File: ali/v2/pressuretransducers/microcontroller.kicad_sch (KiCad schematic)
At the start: 45 parts, among them J1 Conn_02x01, J2 Conn_01x05, J3 USB_C_Receptacle_USB2.0_16P, J4 Conn_01x15, J5 Conn_02x09_Counter_Clockwise, J6 Screw_Terminal_01x02, J7 Screw_Terminal_01x02, SW1 SKRPANE010, U1 STM32H563RIV6, U2 AP2112K-3.3, Y1 25 MHz, Y2 8.192 MHz

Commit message: Globally remove LCSC labels, update MPNs and IOCs, add +5V monitoring to DAQs, fix some footprints
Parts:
- added R8, R9: 10k, APRL_Passive:R_0603, symbol Device:R_Small_US
- J4: renamed from J5; MANUFACTURER Molex -> (none); MPN 503159-1501 -> (none)
- Y2: MANUFACTURER (none) -> SCTF; MPN (none) -> SX3M8.192M20F30TNN
- renumbered C18 to C12, C12 to C13, C13 to C14, C14 to C15, C15 to C16, C16 to C17, C17 to C18, J4 to J5
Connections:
- net +5V: now also R8.1
- net GND: now also R9.2
- net PB2: now also J4.9 (Pin_9); no longer J4.7 (Pin_7)
- net PD11: now also J4.7 (Pin_7); no longer J4.5 (Pin_5)
- net PD12: now also J4.5 (Pin_5); no longer J4.3 (Pin_3)
- net PB13: now reaches U1.35 (PB13)
- net PB13: now also J4.3 (Pin_3)
- net PB1 renamed +5V_SENSE
- net +5V_SENSE: now also R8.2, R9.1; no longer J4.9 (Pin_9)
- no-connect marks 16 -> 15
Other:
- moved on the sheet: C12, D3, D4, D5, J4, R5, R6, R7, Y2

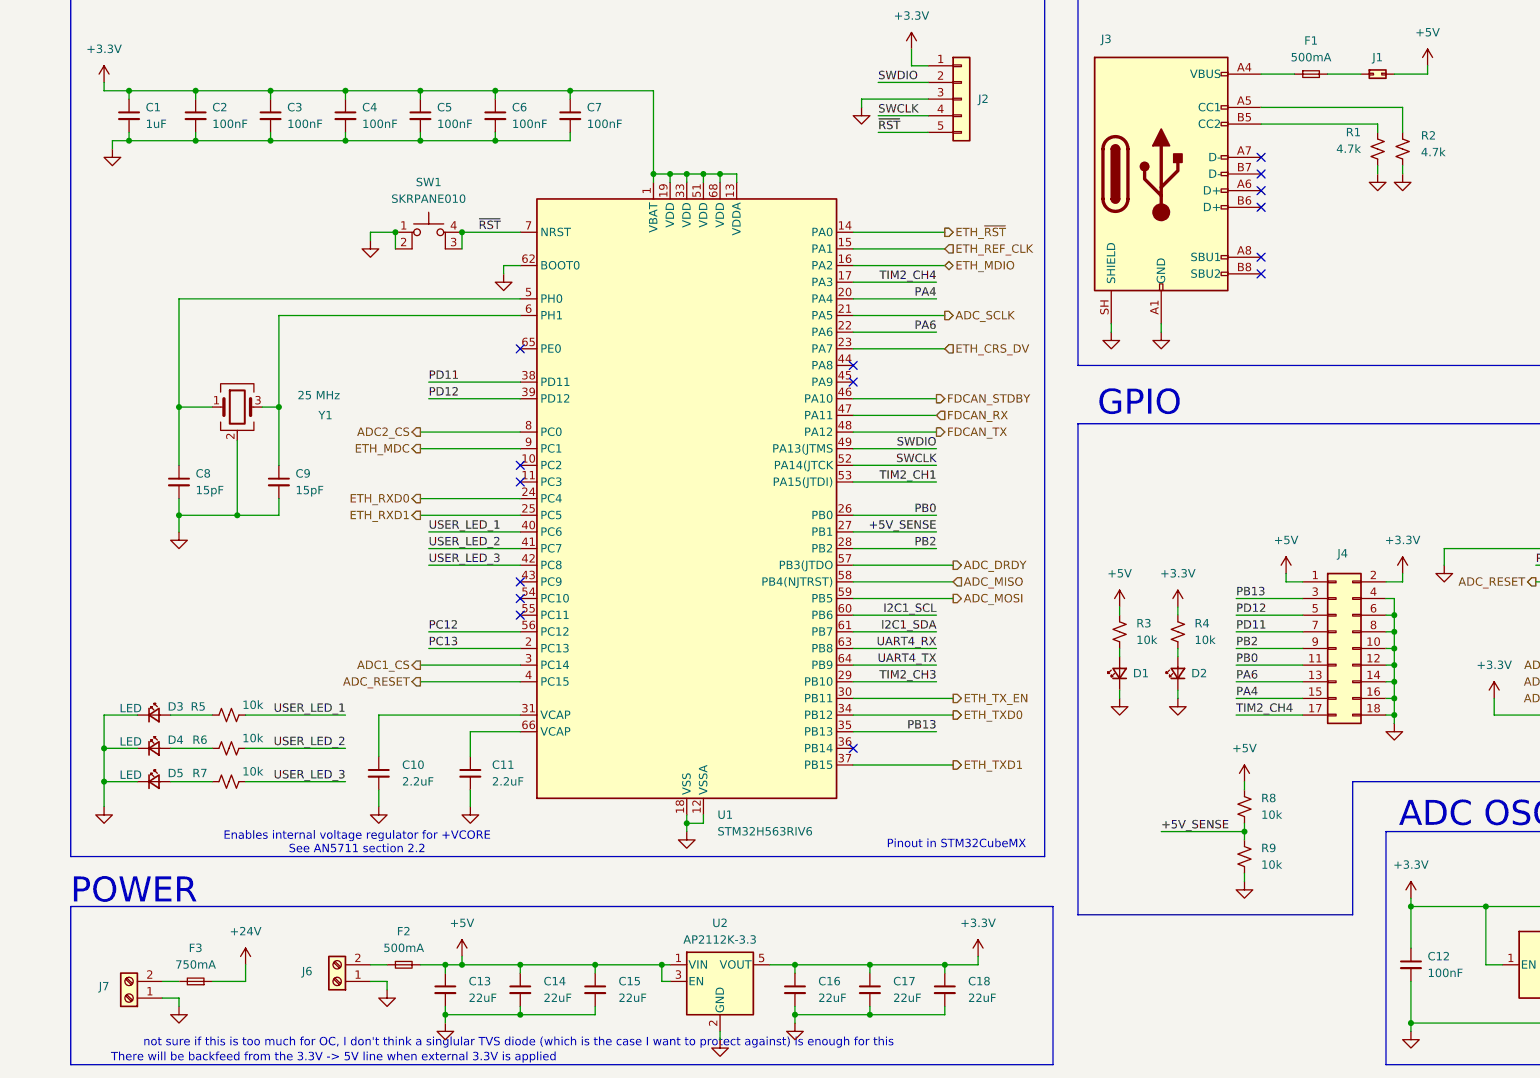
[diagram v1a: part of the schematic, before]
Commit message: the great flatpak and kicad 10.0.6 migration
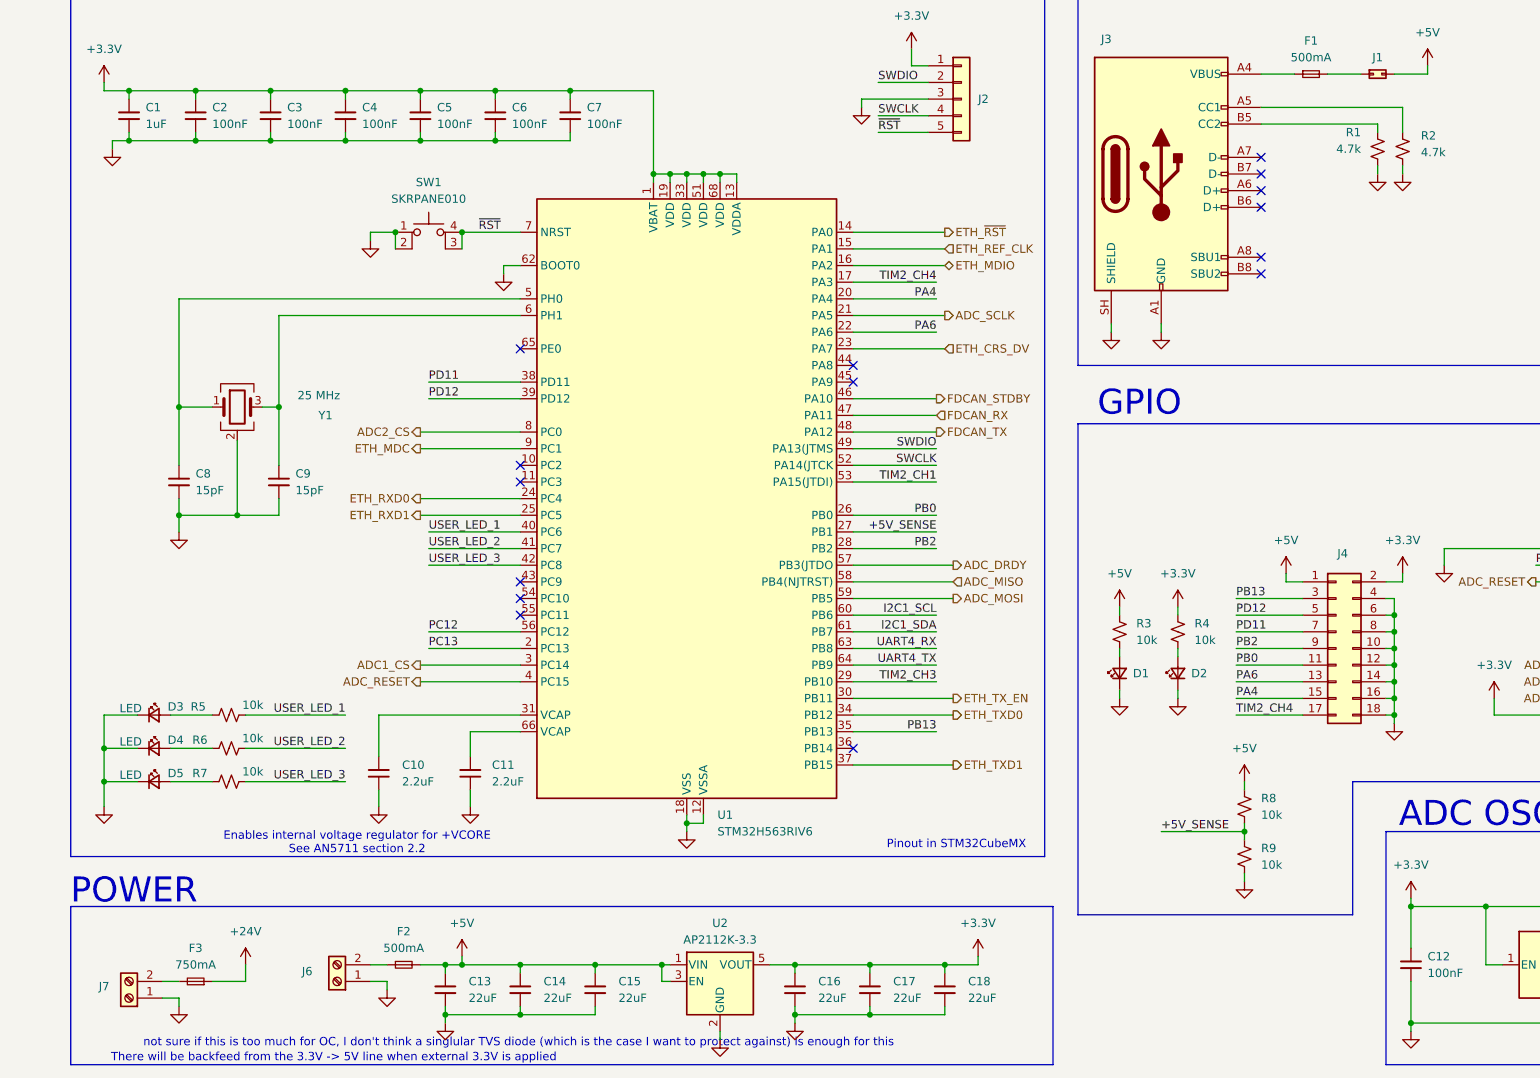
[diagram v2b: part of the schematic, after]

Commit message: The other half of the great 10.0.6 migration
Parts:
- U1: symbol MCU_ST_STM32H5:STM32H563RIVx -> APRL_MCU:STM32H563RIVx
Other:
- note added: "I2C broken out but no pullups on host side"

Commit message: Commentary
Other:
- note added: "I didn't place any pullups/pulldowns on many lines because I think we can just rely on the MCU's options. Additionally, I didn't add test points, as we can selectively untent some vias to act as probe points if we feel the need to."
- note added: "I think that we should agree to make this +3.3V on the debug connector for powering the debugger itself and not the board, as it'll cause backfeed otherwise. It didn't damage the TC board's AP2112K (as far as we know), but if we can avoid it we should."
- note added: "I think the MCU should use its internal ADCs to measure +3.3V (against the internal reference) and temperature. It's not like we're bandwidth bound, and its not as if this would actually hurt anything."
- note added: "So the idea here is that every since ADC shares a start pin and a clock pin, such that they always finish conversions and take measurements at the same time. This also grants better PSRR."
- note added: "The +5V sense pin is for detecting if the +5V rail droops. We have the space, so why not?"
- note added: "The idea behind putting DRDY on timers is that it allows us to use input capture to get exact timestamps, but it's arguably useless without any time sync techniques. It also means that we have to route SPI's SCLK weirdly, as one of the channels lands on it."
- note added: "UART and I2C are broken out because they're there, and not because we specifically need them. It would help if we used one of ST's iolink transcievers, I guess. They'd most likely just be used for CS and Start pins for more adcs."
- note added: "We don't ever use the data lines of USB and they take up a convenient CANBUS space There's a jumper here but not on the other +5V rail because there should be no scenario where USB power would be connected alongside external +5V."

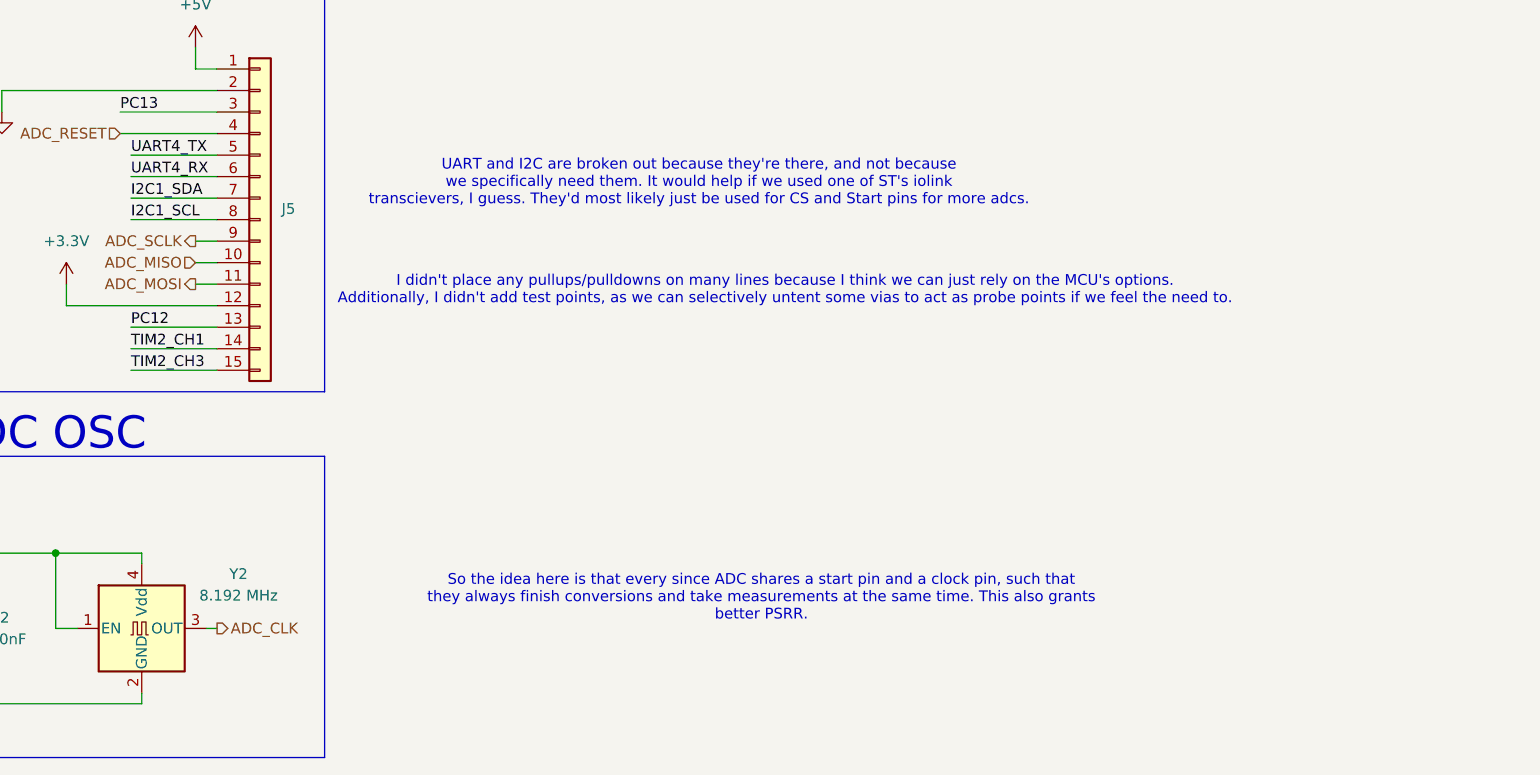
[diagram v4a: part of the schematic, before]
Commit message: Document setup, update template, and use an ampersand when referring to APRL
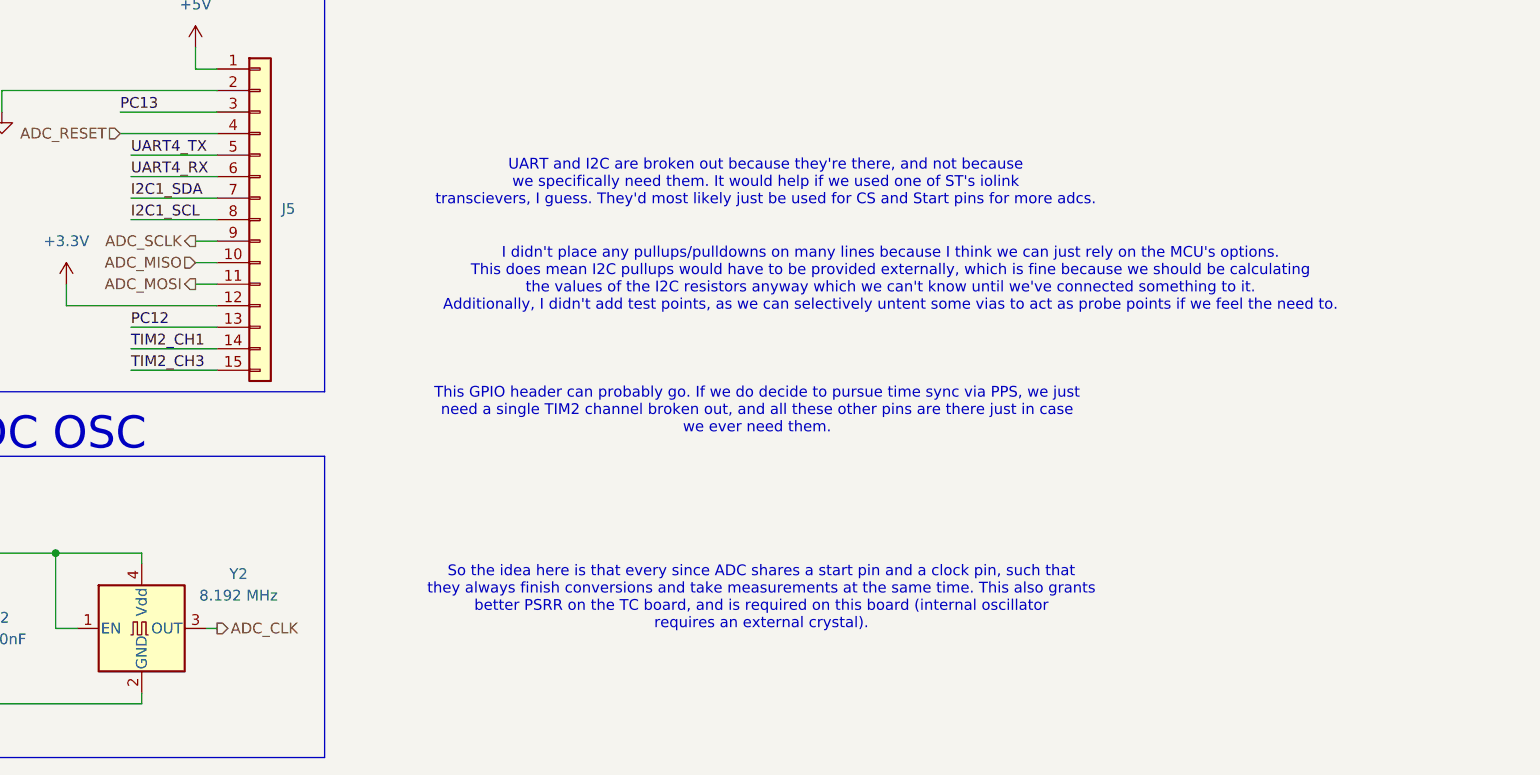
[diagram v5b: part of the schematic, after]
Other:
- note added: "I didn't place any pullups/pulldowns on many lines because I think we can just rely on the MCU's options. This does mean I2C pullups would have to be provided externally, which is fine because we should be calculating the values of the I2C resistors anyway which we can't know until we've connected something to it. Additionally, I didn't add test points, as we can selectively untent some vias to a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"
- note added: "So the idea here is that every since ADC shares a start pin and a clock pin, such that they always finish conversions and take measurements at the same time. This also grants better PSRR on the TC board, and is required on this board (internal oscillator requires an external crystal)."
- note added: "This GPIO header can probably go. If we do decide to pursue time sync via PPS, we just need a single TIM2 channel broken out, and all these other pins are there just in case we ever need them."
- note removed: "I didn't place any pullups/pulldowns on many lines because I think we can just rely on the MCU's options. Additionally, I didn't add test points, as we can selectively untent some vias to act as probe points if we feel the need to."
- note removed: "So the idea here is that every since ADC shares a start pin and a clock pin, such that they always finish conversions and take measurements at the same time. This also grants better PSRR."

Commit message: Begin prep for second board review
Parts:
- removed C12: 100nF, APRL_Passive:C_0603, symbol Device:C_Small
- removed R8, R9: 10k, APRL_Passive:R_0603, symbol Device:R_Small_US
- removed Y2: 8.192 MHz, APRL_Passive:Oscillator_SCTF_SX3M_3.2x2.5mm, symbol APRL_Misc:SX3M-xxxMHz
- R1, R2: value 4.7k -> 5.1k; MPN RC0603FR-074K7L -> RC0603FR-075K1L
- renumbered C13 to C12, C14 to C13, C15 to C14, C16 to C15, C17 to C16, C18 to C17, D3 to D1, D4 to D2, D5 to D3, D1 to D4, D2 to D5, R5 to R3, R6 to R4, R3 to R5, R4 to R6
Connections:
- net +5V_SENSE: no longer names the net of U1.27 (PB1)
- net ADC_DRDY renamed ADC_DRDY1
- net TIM2_CH4: no longer names the net of J4.17 (Pin_17)
- net TIM2_CH4: no longer U1.17 (PA3)
- net USER_LED_1: no longer names the net of R3.2, U1.40 (PC6)
- net USER_LED_2: no longer names the net of R4.2, U1.41 (PC7)
- net USER_LED_3: no longer names the net of R7.2, U1.42 (PC8)
- new net ADC_DRDY2: U1.17 (PA3)
- no-connect marks 15 -> 17
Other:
- note removed: "ADC OSC"
- note removed: "I didn't place any pullups/pulldowns on many lines because I think we can just rely on the MCU's options. This does mean I2C pullups would have to be provided externally, which is fine because we should be calculating the values of the I2C resistors anyway which we can't know until we've connected something to it. Additionally, I didn't add test points, as we can selectively untent some vias to a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"
- note removed: "I think that we should agree to make this +3.3V on the debug connector for powering the debugger itself and not the board, as it'll cause backfeed otherwise. It didn't damage the TC board's AP2112K (as far as we know), but if we can avoid it we should."
- note removed: "I think the MCU should use its internal ADCs to measure +3.3V (against the internal reference) and temperature. It's not like we're bandwidth bound, and its not as if this would actually hurt anything."
- note removed: "So the idea here is that every since ADC shares a start pin and a clock pin, such that they always finish conversions and take measurements at the same time. This also grants better PSRR on the TC board, and is required on this board (internal oscillator requires an external crystal)."
- note removed: "The +5V sense pin is for detecting if the +5V rail droops. We have the space, so why not?"
- note removed: "The idea behind putting DRDY on timers is that it allows us to use input capture to get exact timestamps, but it's arguably useless without any time sync techniques. It also means that we have to route SPI's SCLK weirdly, as one of the channels lands on it."
- note removed: "This GPIO header can probably go. If we do decide to pursue time sync via PPS, we just need a single TIM2 channel broken out, and all these other pins are there just in case we ever need them."
- note removed: "UART and I2C are broken out because they're there, and not because we specifically need them. It would help if we used one of ST's iolink transcievers, I guess. They'd most likely just be used for CS and Start pins for more adcs."
- note removed: "We don't ever use the data lines of USB and they take up a convenient CANBUS space There's a jumper here but not on the other +5V rail because there should be no scenario where USB power would be connected alongside external +5V."
- note removed: "not sure if this is too much for OC, I don't think a singlular TVS diode (which is the case I want to protect against) is enough for this"
- moved on the sheet: D1, D2, D3, R3, R4, R7
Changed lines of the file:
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@@
 	(paper "USLetter")
 	(title_block
-		(date "2026-09-11")
+		(date "2026-10-10")
 	)
